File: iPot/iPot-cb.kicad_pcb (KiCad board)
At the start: 2 copper layers, 100 x 100 mm, 65 parts, among them CON1 12VDC, IC1 ATMEGA644-P, IC2 L298, P1 MOT2, P10 I2C3, P11 I2C4, P12 UART, P13 USB_PWR2, P14 ANALOG_IN, P15 PWM_IO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

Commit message: Fix connector orientation
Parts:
- moved P1 5.08 mm to (55.9, 91.4), turned to 270 degrees
- moved P2 5.08 mm to (55.9, 80.0), turned to 270 degrees
- renumbered REF** to MHOLE1, REF** to MHOLE2, REF** to MHOLE3, REF** to MHOLE4, REF** to OSHW_LOGO
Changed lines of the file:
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@@
     (links 170)
     (no_connects 170)
-    (area 49.53 49.53 149.86 149.86)
+    (area 49.949999 49.949999 150.050001 150.050001)
     (thickness 1.6)
     (drawings 4)
@@
   )
   (module Terminal_Blocks:TerminalBlock_Pheonix_MKDS1.5-2pol locked (layer F.Cu)
-    (at 55.88 96.52 90)
+    (at 55.88 91.44 270)
     (descr "2-way 5mm pitch terminal block, Phoenix MKDS series")
-    (fp_text reference P1 (at 2.5 5.9 90) (layer F.SilkS)
-      (effects (font (size 1 1) (thickness 0.15)))
-    )
-    (fp_text value MOT2 (at 2.5 -6.6 90) (layer F.Fab)
+    (fp_text reference P1 (at 2.5 5.9 270) (layer F.SilkS)
+      (effects (font (size 1 1) (thickness 0.15)))
+    )
+    (fp_text value MOT2 (at 2.5 -6.6 270) (layer F.Fab)
       (effects (font (size 1 1) (thickness 0.15)))
     )
@@
     (fp_line (start 7.5 -5.2) (end -2.5 -5.2) (layer F.SilkS) (width 0.15))
     (fp_line (start -2.5 -5.2) (end -2.5 4.6) (layer F.SilkS) (width 0.15))
-    (pad 1 thru_hole rect (at 0 0 90) (size 2.5 2.5) (drill 1.3) (layers *.Cu *.Mask F.SilkS)
+    (pad 1 thru_hole rect (at 0 0 270) (size 2.5 2.5) (drill 1.3) (layers *.Cu *.Mask F.SilkS)
       (net 13 "Net-(D10-Pad2)"))
-    (pad 2 thru_hole circle (at 5 0 90) (size 2.5 2.5) (drill 1.3) (layers *.Cu *.Mask F.SilkS)
+    (pad 2 thru_hole circle (at 5 0 270) (size 2.5 2.5) (drill 1.3) (layers *.Cu *.Mask F.SilkS)
       (net 12 "Net-(D5-Pad1)"))
     (model Terminal_Blocks.3dshapes/TerminalBlock_Pheonix_MKDS1.5-2pol.wrl
@@
   )
   (module Terminal_Blocks:TerminalBlock_Pheonix_MKDS1.5-2pol locked (layer F.Cu)
-    (at 55.88 85.09 90)
+    (at 55.88 80.01 270)
     (descr "2-way 5mm pitch terminal block, Phoenix MKDS series")
-    (fp_text reference P2 (at 2.5 5.9 90) (layer F.SilkS)
-      (effects (font (size 1 1) (thickness 0.15)))
-    )
-    (fp_text value MOT1 (at 2.5 -6.6 90) (layer F.Fab)
+    (fp_text reference P2 (at 2.5 5.9 270) (layer F.SilkS)
+      (effects (font (size 1 1) (thickness 0.15)))
+    )
+    (fp_text value MOT1 (at 2.5 -6.6 270) (layer F.Fab)
       (effects (font (size 1 1) (thickness 0.15)))
     )
@@
     (fp_line (start 7.5 -5.2) (end -2.5 -5.2) (layer F.SilkS) (width 0.15))
     (fp_line (start -2.5 -5.2) (end -2.5 4.6) (layer F.SilkS) (width 0.15))
-    (pad 1 thru_hole rect (at 0 0 90) (size 2.5 2.5) (drill 1.3) (layers *.Cu *.Mask F.SilkS)
+    (pad 1 thru_hole rect (at 0 0 270) (size 2.5 2.5) (drill 1.3) (layers *.Cu *.Mask F.SilkS)
       (net 11 "Net-(D4-Pad1)"))
-    (pad 2 thru_hole circle (at 5 0 90) (size 2.5 2.5) (drill 1.3) (layers *.Cu *.Mask F.SilkS)
+    (pad 2 thru_hole circle (at 5 0 270) (size 2.5 2.5) (drill 1.3) (layers *.Cu *.Mask F.SilkS)
       (net 10 "Net-(D3-Pad1)"))
     (model Terminal_Blocks.3dshapes/TerminalBlock_Pheonix_MKDS1.5-2pol.wrl
@@
     (descr "Mounting hole, Befestigungsbohrung, 3mm, No Annular, Kein Restring,")
     (tags "Mounting hole, Befestigungsbohrung, 3mm, No Annular, Kein Restring,")
-    (fp_text reference REF** (at 0 -4.0005) (layer F.SilkS)
+    (fp_text reference MHOLE3 (at 0 -4.0005) (layer F.SilkS)
       (effects (font (size 1 1) (thickness 0.15)))
     )
@@
     (descr "Mounting hole, Befestigungsbohrung, 3mm, No Annular, Kein Restring,")
     (tags "Mounting hole, Befestigungsbohrung, 3mm, No Annular, Kein Restring,")
-    (fp_text reference REF** (at 0 -4.0005) (layer F.SilkS)
+    (fp_text reference MHOLE2 (at 0 -4.0005) (layer F.SilkS)
       (effects (font (size 1 1) (thickness 0.15)))
     )
@@
     (descr "Mounting hole, Befestigungsbohrung, 3mm, No Annular, Kein Restring,")
     (tags "Mounting hole, Befestigungsbohrung, 3mm, No Annular, Kein Restring,")
-    (fp_text reference REF** (at 0 -4.0005) (layer F.SilkS)
+    (fp_text reference MHOLE4 (at 0 -4.0005) (layer F.SilkS)
       (effects (font (size 1 1) (thickness 0.15)))
     )
@@
     (descr "Mounting hole, Befestigungsbohrung, 3mm, No Annular, Kein Restring,")
     (tags "Mounting hole, Befestigungsbohrung, 3mm, No Annular, Kein Restring,")
-    (fp_text reference REF** (at 0 -4.0005) (layer F.SilkS)
+    (fp_text reference MHOLE1 (at 0 -4.0005) (layer F.SilkS)
       (effects (font (size 1 1) (thickness 0.15)))
     )
@@
     (descr "Symbol, OSHW-Logo, Copper Top, BIG")
     (tags "Symbol, OSHW-Logo, Copper Top, BIG")
-    (fp_text reference REF** (at -0.29972 11.50112) (layer F.SilkS)
-      (effects (font (size 1 1) (thickness 0.15)))
-    )
+    (fp_text reference OSHW_LOGO (at -0.29972 11.50112) (layer F.SilkS)
+      (effects (font (size 1 1) (thickness 0.15)))
+    )

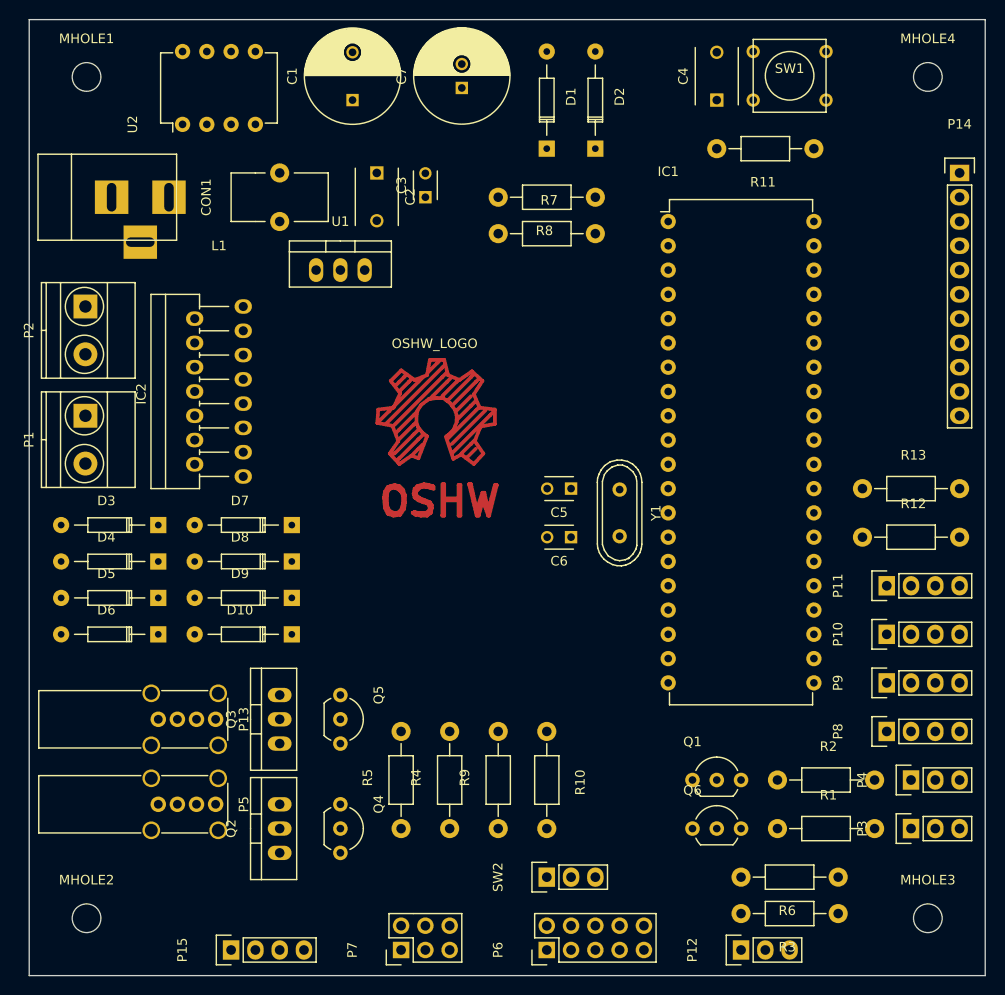
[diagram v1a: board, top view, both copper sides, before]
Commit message: Add autoroute result. (TODO: Copper pour on GND)
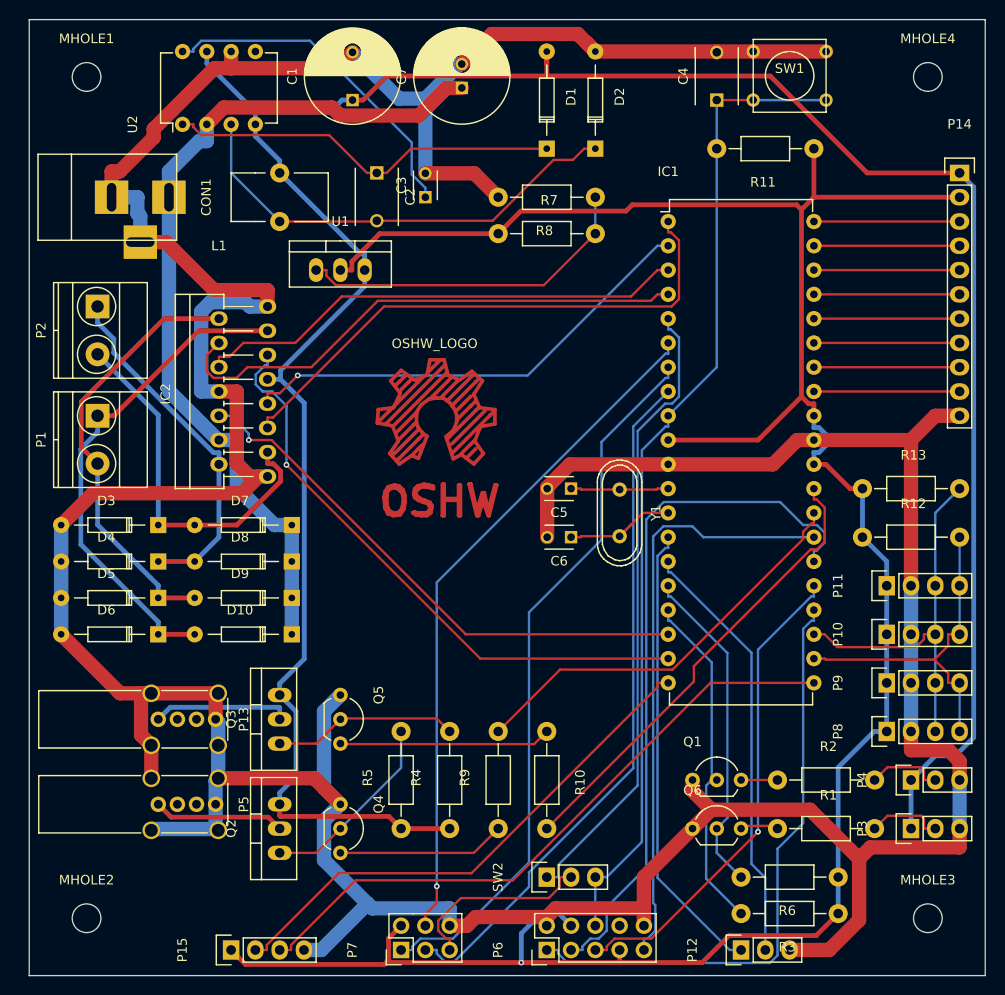
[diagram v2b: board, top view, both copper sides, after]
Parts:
- moved IC2 2.54 mm to (74.9, 97.8)
- moved P1 1.27 mm to (57.1, 91.4)
- moved P2 1.27 mm to (57.1, 80.0)
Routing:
- net GND: track 0.00 -> 489.8 mm
- net +5V: track 0.00 -> 270.3 mm
- net +3V3: track 0.00 -> 255.1 mm, vias 0 -> 1
- net /RST: track 0.00 -> 103.9 mm
- net +12V: track 0.00 -> 91.9 mm
- net /MISO: track 0.00 -> 75.4 mm
- net /TDO: track 0.00 -> 73.9 mm
- net /SCK: track 0.00 -> 72.6 mm
- net /MOSI: track 0.00 -> 71.6 mm, vias 0 -> 1
- net Net-(IC1-Pad21): track 0.00 -> 67.8 mm
- net //SS: track 0.00 -> 65.9 mm
- net /TCK: track 0.00 -> 63.1 mm
- net /MOT2PWM: track 0.00 -> 62.4 mm, vias 0 -> 1
- net /TDI: track 0.00 -> 61.8 mm
- net /MOT1F: track 0.00 -> 58.0 mm
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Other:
- net class GND added: clearance 0.2, trace_width 1.5, via_dia 0.6, via_drill 0.4
- net class MOTOR added: clearance 0.2, trace_width 0.5, via_dia 0.6, via_drill 0.4
- net class Power12V added: clearance 0.2, trace_width 1.5, via_dia 0.6, via_drill 0.4
- net class Power3V3 added: clearance 0.2, trace_width 0.5, via_dia 0.6, via_drill 0.4
- net class Power5V added: clearance 0.2, trace_width 0.5, via_dia 0.6, via_drill 0.4
- net class USB_PWR added: clearance 0.2, trace_width 0.5, via_dia 0.6, via_drill 0.4

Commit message: Finalized layout
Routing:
- net GND: track 489.8 -> 0.00 mm
- net /TDO: track 73.9 -> 51.5 mm, vias 0 -> 1
- net /MOT2PWM: track 62.4 -> 73.8 mm, vias 1 -> 0
- net Net-(D3-Pad1): track 39.1 -> 47.0 mm
- net /MOT2R: track 55.6 -> 49.1 mm
- net +3V3: track 255.1 -> 248.8 mm, vias 1 -> 0
- net Net-(P7-Pad5): track 20.2 -> 15.9 mm
- net /MOT1F: track 58.0 -> 54.4 mm
- net /SCK: track 72.6 -> 70.1 mm
- net Net-(D10-Pad2): track 52.2 -> 50.1 mm
- net Net-(C3-Pad1): track 35.3 -> 33.3 mm
- net Net-(C6-Pad1): track 12.9 -> 11.2 mm
- net +5V: track 270.3 -> 268.8 mm
- net +12V: track 91.9 -> 90.5 mm
- net /MISO: track 75.4 -> 74.0 mm
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- added copper zone on B.Cu, net GND
- added copper zone on F.Cu, net GND

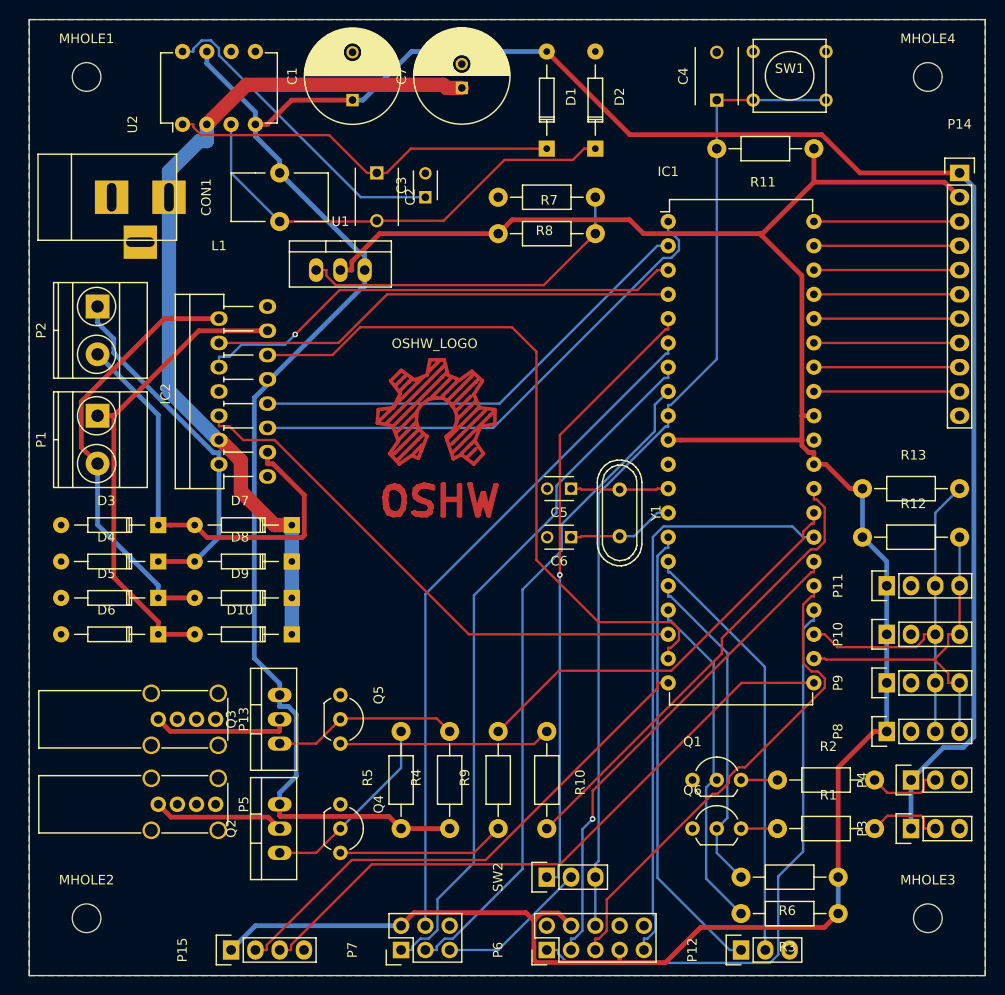
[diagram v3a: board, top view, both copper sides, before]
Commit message: Fix possible problems, bump version 1.1
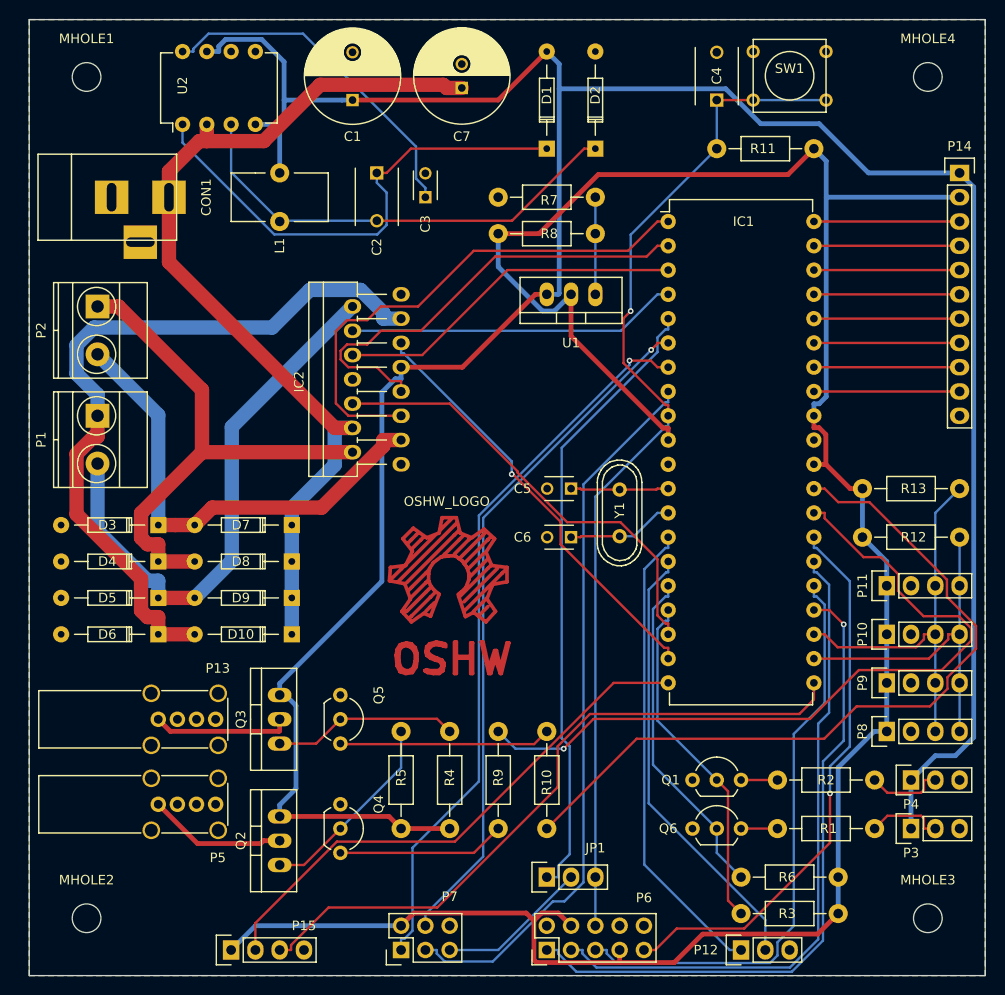
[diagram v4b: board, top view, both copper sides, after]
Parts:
- removed SW2: ISP_SELECT_JP, Pin_Headers:Pin_Header_Straight_1x03
- added JP1: ISP_SELECT_JP, Pin_Headers:Pin_Header_Straight_1x03, F.Cu at (104.1, 139.7)
- Q2, Q3: value IRF630 -> IRF9610
- moved U1 24.3 mm to (106.7, 78.7), turned to 180 degrees
- moved OSHW_LOGO 16.6 mm to (94.0, 88.9)
- moved IC2 14.0 mm to (88.9, 96.5)
- moved Q2 1.27 mm to (76.2, 135.9)
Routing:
- net /USB1: track 43.6 -> 79.0 mm, vias 0 -> 1
- net /USB2: track 48.6 -> 79.7 mm
- net /MOT2PWM: track 73.8 -> 45.1 mm, vias 0 -> 1
- net Net-(D10-Pad2): track 50.1 -> 78.3 mm
- net Net-(R7-Pad2): track 36.2 -> 10.2 mm
- net +5V: track 268.8 -> 290.9 mm
- net Net-(D4-Pad1): track 37.1 -> 56.1 mm
- net /TDO: track 51.5 -> 68.9 mm, vias 1 -> 0
- net /MOT2F: track 51.8 -> 36.7 mm, vias 1 -> 0
- net /MOT2R: track 49.1 -> 34.6 mm
- net Net-(D5-Pad1): track 45.7 -> 58.5 mm
- net Net-(C2-Pad1): track 41.4 -> 52.3 mm
- net /TMS: track 50.9 -> 61.5 mm
- net /MOT1PWM: track 57.1 -> 47.2 mm
- net +12V: track 90.5 -> 97.5 mm
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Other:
- net class MOTOR: trace_width 0.5 -> 1.5

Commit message: Add heatsink
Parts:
- added HS1: HEATSINK, SY403B:SY403B, F.Cu at (78.7, 87.6)
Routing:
- net Net-(D4-Pad1): track 56.1 -> 60.4 mm
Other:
- board text added: "iPot control board v1.1. released under CERN OHL v1.2 or later."

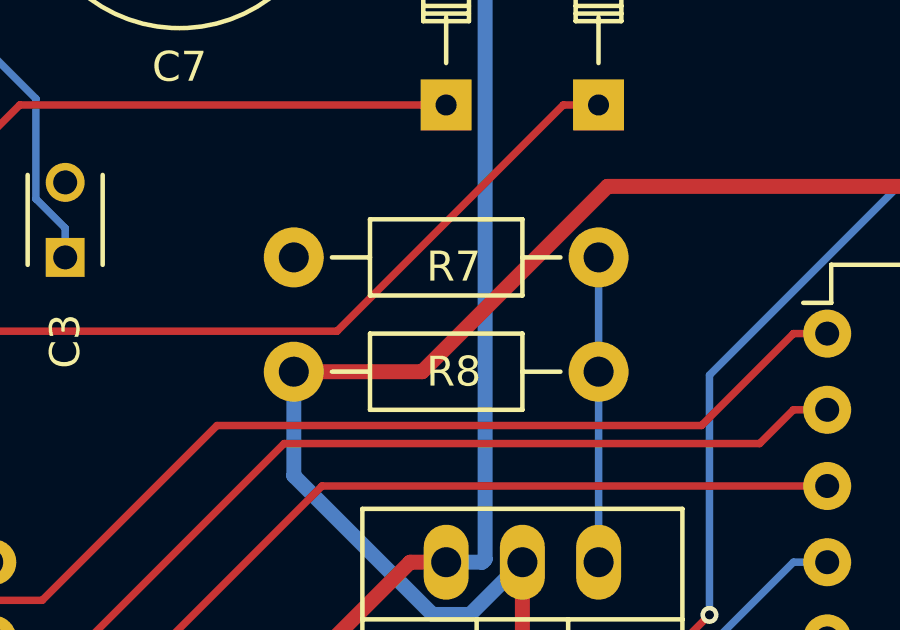
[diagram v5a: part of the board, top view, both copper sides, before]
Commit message: Fix bug in silk, fix resistor value, bump version to 1.2
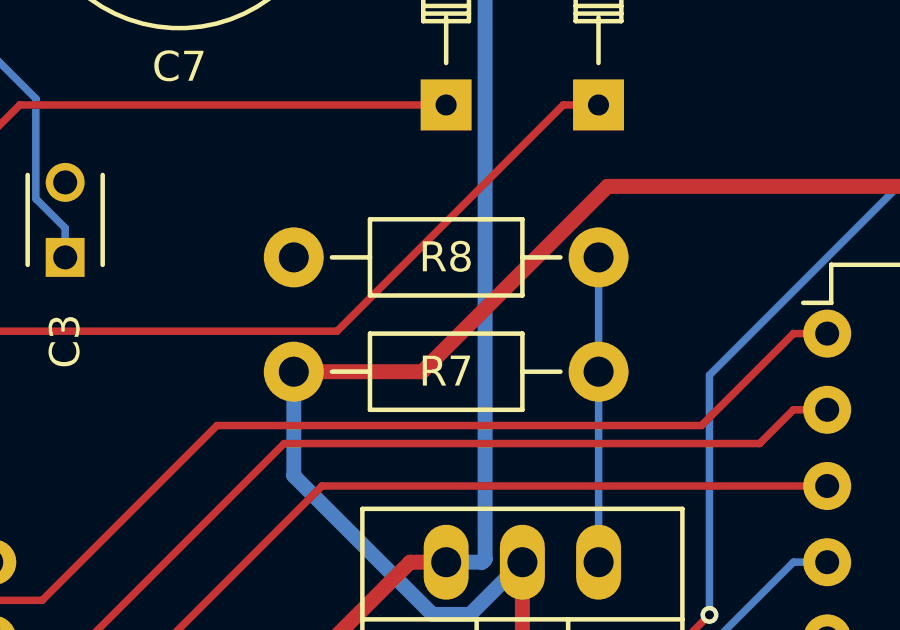
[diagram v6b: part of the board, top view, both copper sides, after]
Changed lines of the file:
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@@
     (links 170)
     (no_connects 1)
-    (area 49.949999 49.949999 150.050001 150.050001)
+    (area 49.511474 49.949999 152.490046 150.380714)
     (thickness 1.6)
     (drawings 5)
@@
     (title "iPot control board")
     (date 2016-05-04)
-    (rev v1.1)
+    (rev v1.2)
     (company "Korea University")
     (comment 1 "Licensed under CERN OHL v1.2")
@@
     (descr "Resistor, Axial,  RM 10mm, 1/3W")
     (tags "Resistor Axial RM 10mm 1/3W")
-    (fp_text reference R7 (at 5.32892 -3.50012) (layer F.SilkS)
+    (fp_text reference R7 (at 5.08 0) (layer F.SilkS)
       (effects (font (size 1 1) (thickness 0.15)))
     )
@@
     (descr "Resistor, Axial,  RM 10mm, 1/3W")
     (tags "Resistor Axial RM 10mm 1/3W")
-    (fp_text reference R8 (at 4.826 -3.81 180) (layer F.SilkS)
-      (effects (font (size 1 1) (thickness 0.15)))
-    )
+    (fp_text reference R8 (at 5.08 0 180) (layer F.SilkS)
+      (effects (font (size 1 1) (thickness 0.15)))
+    )
